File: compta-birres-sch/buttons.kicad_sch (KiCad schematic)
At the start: 9 parts, among them SW1 SW_Push, SW2 SW_Push, SW3 SW_Push, SW4 SW_Push, SW5 SW_Push, SW6 SW_Push, SW7 SW_Push, SW8 SW_Push, U7 74HC4051

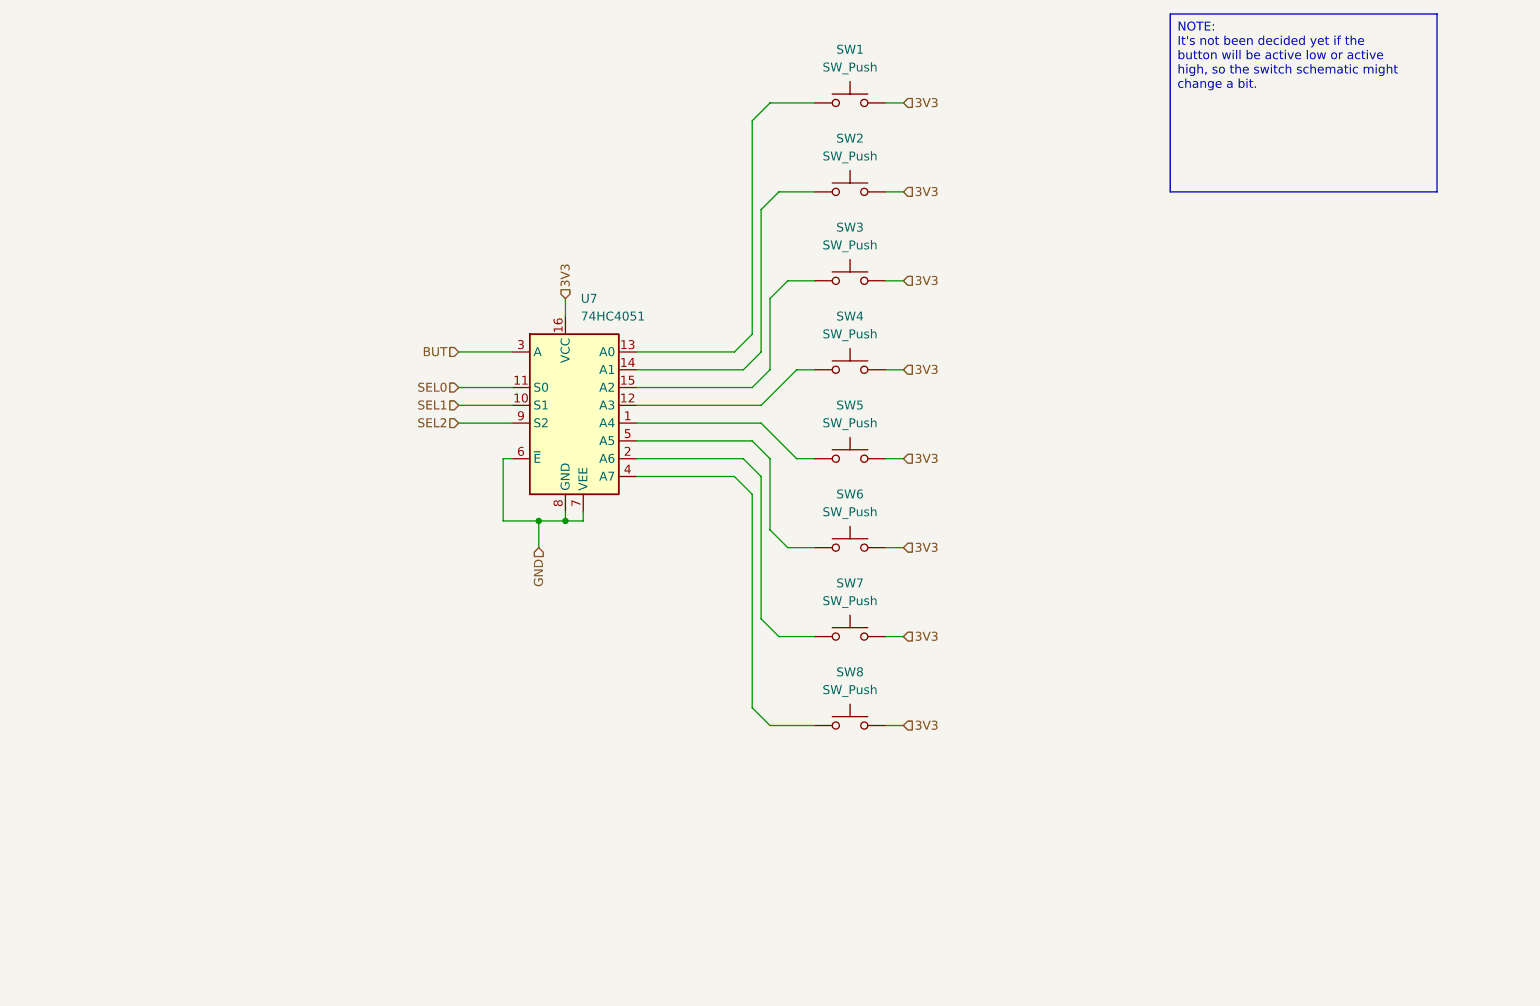
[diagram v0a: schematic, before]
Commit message: Updated schematics for buttons
Use push buttons with a pullup and add capacitor for reducing interferences.
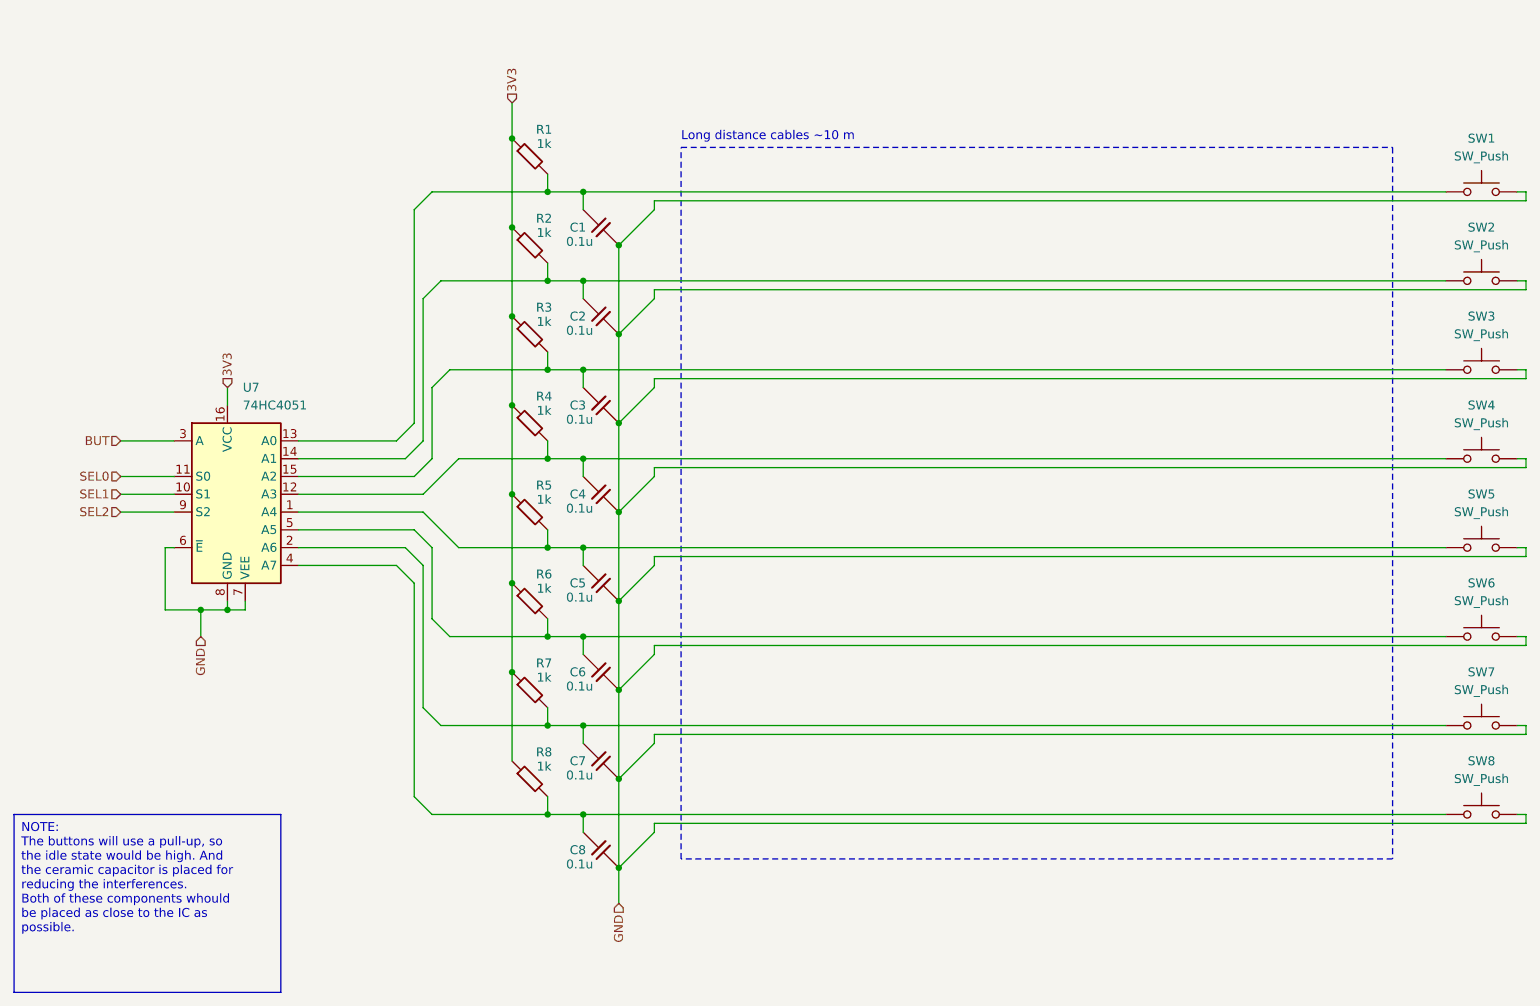
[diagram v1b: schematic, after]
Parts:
- added C1, C2, C3, C4, C5, C6, C7, C8: 0.1u, symbol Device:C_45deg
- added R1, R2, R3, R4, R5, R6, R7, R8: 1k, symbol Device:R_45deg
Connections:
- net 3V3: now also R1.1, R2.1, R3.1, R4.1, R5.1, R6.1, R7.1, R8.1; no longer SW1.2, SW2.2, SW3.2, SW4.2, SW5.2, SW6.2, SW7.2, SW8.2
- net GND: now also SW1.2, SW2.2, SW3.2, SW4.2, SW5.2, SW6.2, SW7.2, SW8.2, C1.1, C2.1, C3.1, C4.1, C5.1, C6.1, C7.1, C8.1
- net at SW5.1, U7.1 (A4): now also C5.2, R5.2
- net at SW4.1, U7.12 (A3): now also C4.2, R4.2
- net at SW3.1, U7.15 (A2): now also C3.2, R3.2
- net at SW6.1, U7.5 (A5): now also C6.2, R6.2
- net at SW2.1, U7.14 (A1): now also C2.2, R2.2
- net at SW7.1, U7.2 (A6): now also C7.2, R7.2
- net at SW1.1, U7.13 (A0): now also C1.2, R1.2
- net at SW8.1, U7.4 (A7): now also C8.2, R8.2
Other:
- note added: "Long distance cables ~10 m"
- moved on the sheet: U7
